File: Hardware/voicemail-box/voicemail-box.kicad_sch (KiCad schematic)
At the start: 13 parts, among them J1 Power, J2 Digital/PWM, J3 Analog, J4 Digital/PWM, J5 Conn_02x06_Top_Bottom, U1 ESP32-WROOM-32

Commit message: + gitignore ~ added existing pinout of sandbox tests
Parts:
- removed J1: Power, Connector_PinSocket_2.54mm:PinSocket_1x08_P2.54mm_Vertical, symbol Connector_Generic:Conn_01x08
- removed J2: Digital/PWM, Connector_PinSocket_2.54mm:PinSocket_1x10_P2.54mm_Vertical, symbol Connector_Generic:Conn_01x10
- removed J3: Analog, Connector_PinSocket_2.54mm:PinSocket_1x06_P2.54mm_Vertical, symbol Connector_Generic:Conn_01x06
- removed J4: Digital/PWM, Connector_PinSocket_2.54mm:PinSocket_1x08_P2.54mm_Vertical, symbol Connector_Generic:Conn_01x08
- added C3: 100n, Capacitor_SMD:C_0805_2012Metric_Pad1.18x1.45mm_HandSolder, symbol Device:C
- added CN1: ~, Connector_PinSocket_2.54mm:PinSocket_2x15_P2.54mm_Vertical, symbol myParts:NUCLEO_144_Analog+
- added CN2: ~, Connector_PinSocket_2.54mm:PinSocket_2x17_P2.54mm_Vertical, symbol myParts:NUCLEO_144_GPIO+
- added CN3: ~, Connector_PinSocket_2.54mm:PinSocket_2x10_P2.54mm_Vertical, symbol myParts:NUCLEO_144_Periphery+
- added CN4: ~, Connector_PinSocket_2.54mm:PinSocket_2x08_P2.54mm_Vertical, symbol myParts:NUCLEO_144_Power
- added J6: Micro_SD_Card_Det1, symbol Connector:Micro_SD_Card_Det1
- added RN3: 10k, Resistor_SMD:R_Array_Convex_4x0603, symbol Device:R_Pack04
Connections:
- net +3V3: now also C3.1, CN4.1 (NC), CN4.5 (NRST), J6.4 (VDD), RN3.1 (R1.1), RN3.2 (R2.1), RN3.3 (R3.1), RN3.4 (R4.1)
- net +5V: now also CN4.7 (+3V3)
- net AREF: now also CN3.6 (VREFP)
- net D2: now also CN2.12 (D2)
- net D3: now also CN2.10 (D3)
- net D4: now also CN2.8 (D4)
- net D5: now also CN2.6 (D5)
- net D6: now also CN2.4 (D6)
- net D8: now also CN3.20 (D8)
- net D9: now also CN3.18 (D9)
- net GND: now also C3.2, CN1.12 (GND), CN1.23 (GND), CN2.17 (GND), CN2.22 (GND), CN2.27 (GND), CN2.3 (AGND), CN2.5 (GND), CN3.8 (GND), CN4.11 (GND), CN4.9 (+5V), J6.10 (SHIELD), J6.6 (VSS)
- net RX/D0: now also CN2.16 (D0)
- net TX/D1: now also CN2.14 (D1)
- net VCC: now also CN4.13 (GND)
- net ~{RESET}: now also CN4.3 (IOREF)
- new net NFC_LED1: CN1.3 (A1)
- new net NFC_LED2: CN1.5 (A2)
- new net NFC_LED3: CN1.7 (A3)
- new net NFC_LED4: CN1.9 (A4)
- new net NFC_LED5: CN1.11 (A5)
- new net NFC_LED6: CN2.2 (D7)
- new net NFC_MISO: CN3.12 (D12)
- new net NFC_MOSI: CN3.14 (D11)
- new net NFC_NSS: CN3.16 (D10)
- new net NFC_SCK: CN3.10 (D13)
- new net NFT_INT: CN1.1 (A0)
- new net SCL: CN3.2 (D15)
- new net SDA: CN3.4 (D14)
- new net SD_CLK: CN4.10 (D47), J6.5 (CLK)
- new net SD_CMD: CN4.12 (D48), J6.3 (CMD)
- new net SD_DAT0: CN4.2 (D43), J6.7 (DAT0), RN3.5 (R4.2)
- new net SD_DAT1: CN4.4 (D44), J6.8 (DAT1), RN3.6 (R3.2)
- new net SD_DAT2: CN4.6 (D45), J6.1 (DAT2), RN3.7 (R2.2)
- new net SD_DAT3: CN4.8 (D46), J6.2 (DAT3/CD), RN3.8 (R1.2)
- new net SD_DET: CN4.14 (D49), J6.9 (DET)
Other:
- note added: "ESD-Protection for production Version required"
- note added: "F469 | H755"
- note added: "H755"
- note added: "Left out for ease of soldering for inexperienced users"
- note added: "Micro SD-Card"
- note added: "PA3 | PB1"
- note added: "PA5 | PD3"
- note added: "PA6 | PB14"
- note added: "PB1 | PC4"
- note added: "PB5 | PB15"
- note added: "PB8 | PB8"
- note added: "PB9 | PB9"
- note added: "PC0 | PC2"
- note added: "PC10"
- note added: "PC11"
- note added: "PC12"
- note added: "PC2 | PC5"
- note added: "PC3 | PC3"
- note added: "PC8"
- note added: "PC9"
- note added: "PD14 | PH6"
- note added: "PD2"
- note added: "PF11 | PA4"
- note added: "PG10"
- note added: "PG12 | PG11"
- note removed: "* Indicates a PWM-capable pin"
- note removed: "A0 | PA3 | PB1"
- note removed: "A1 | PC0 | PC2"
- note removed: "A2 | PC3 | PC3"
- note removed: "A3 | PB1 | PC4"
- note removed: "A4 | PC2 | PC5"
- note removed: "A5 | PF11 | PA4"
- note removed: "D14 | PB9 | PB9"
- note removed: "D15 | PB8 | PB8"

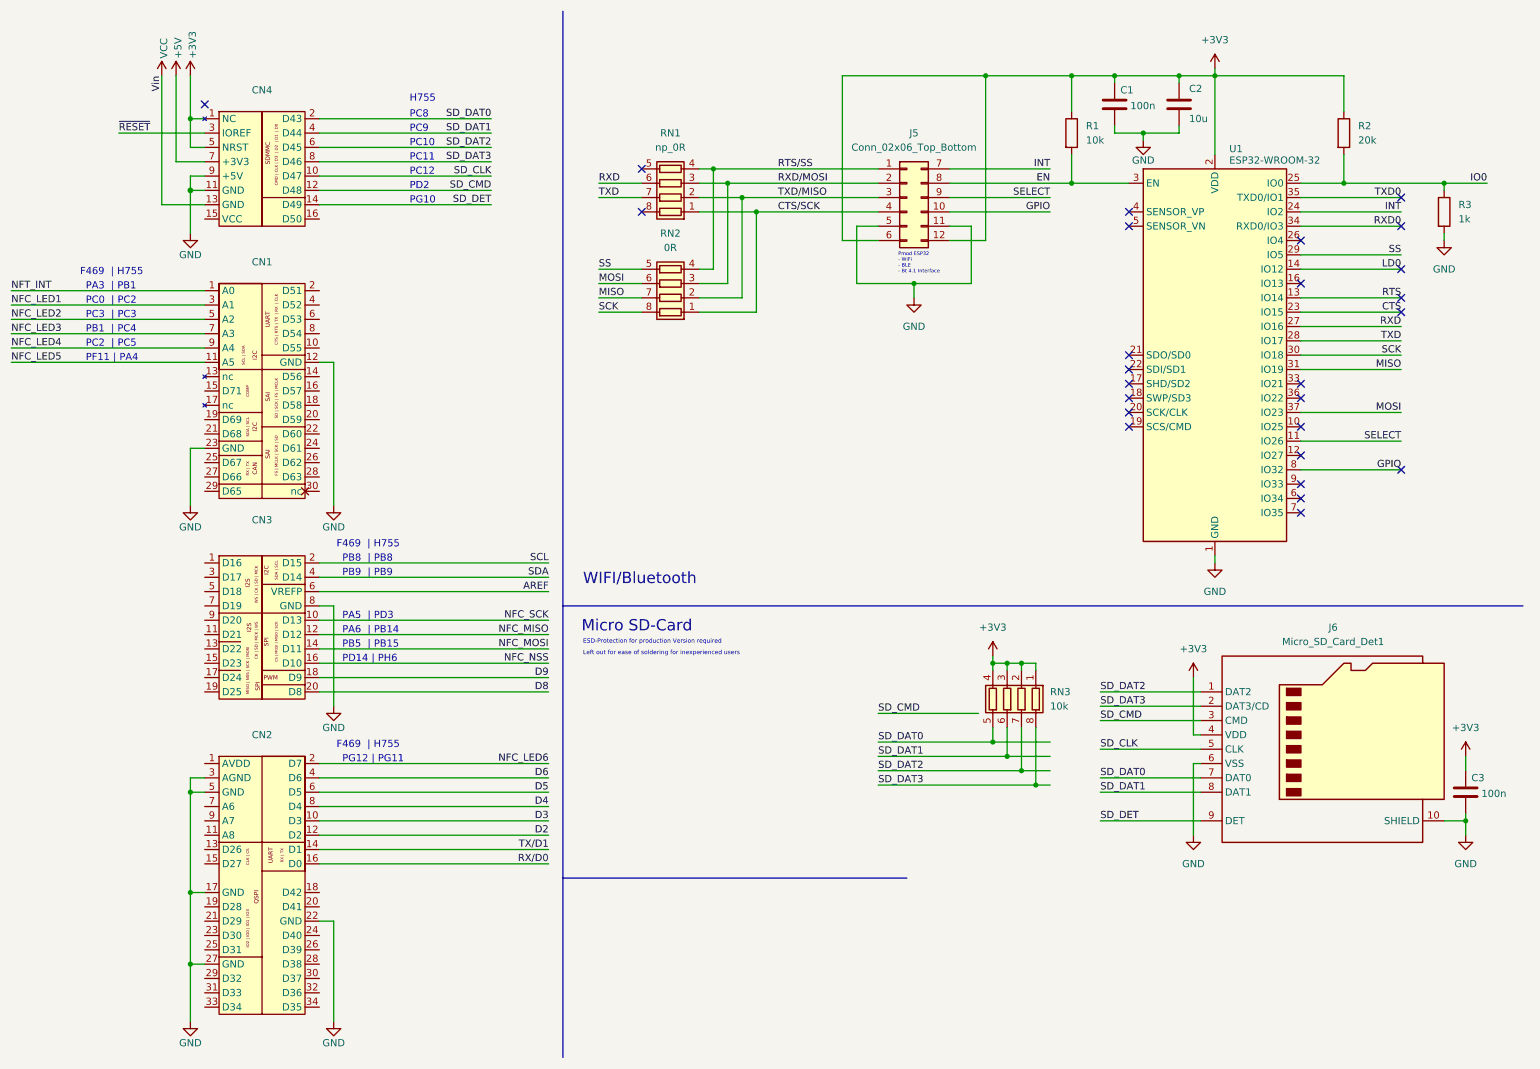
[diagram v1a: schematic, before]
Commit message: ~changed to hierarchical schematic
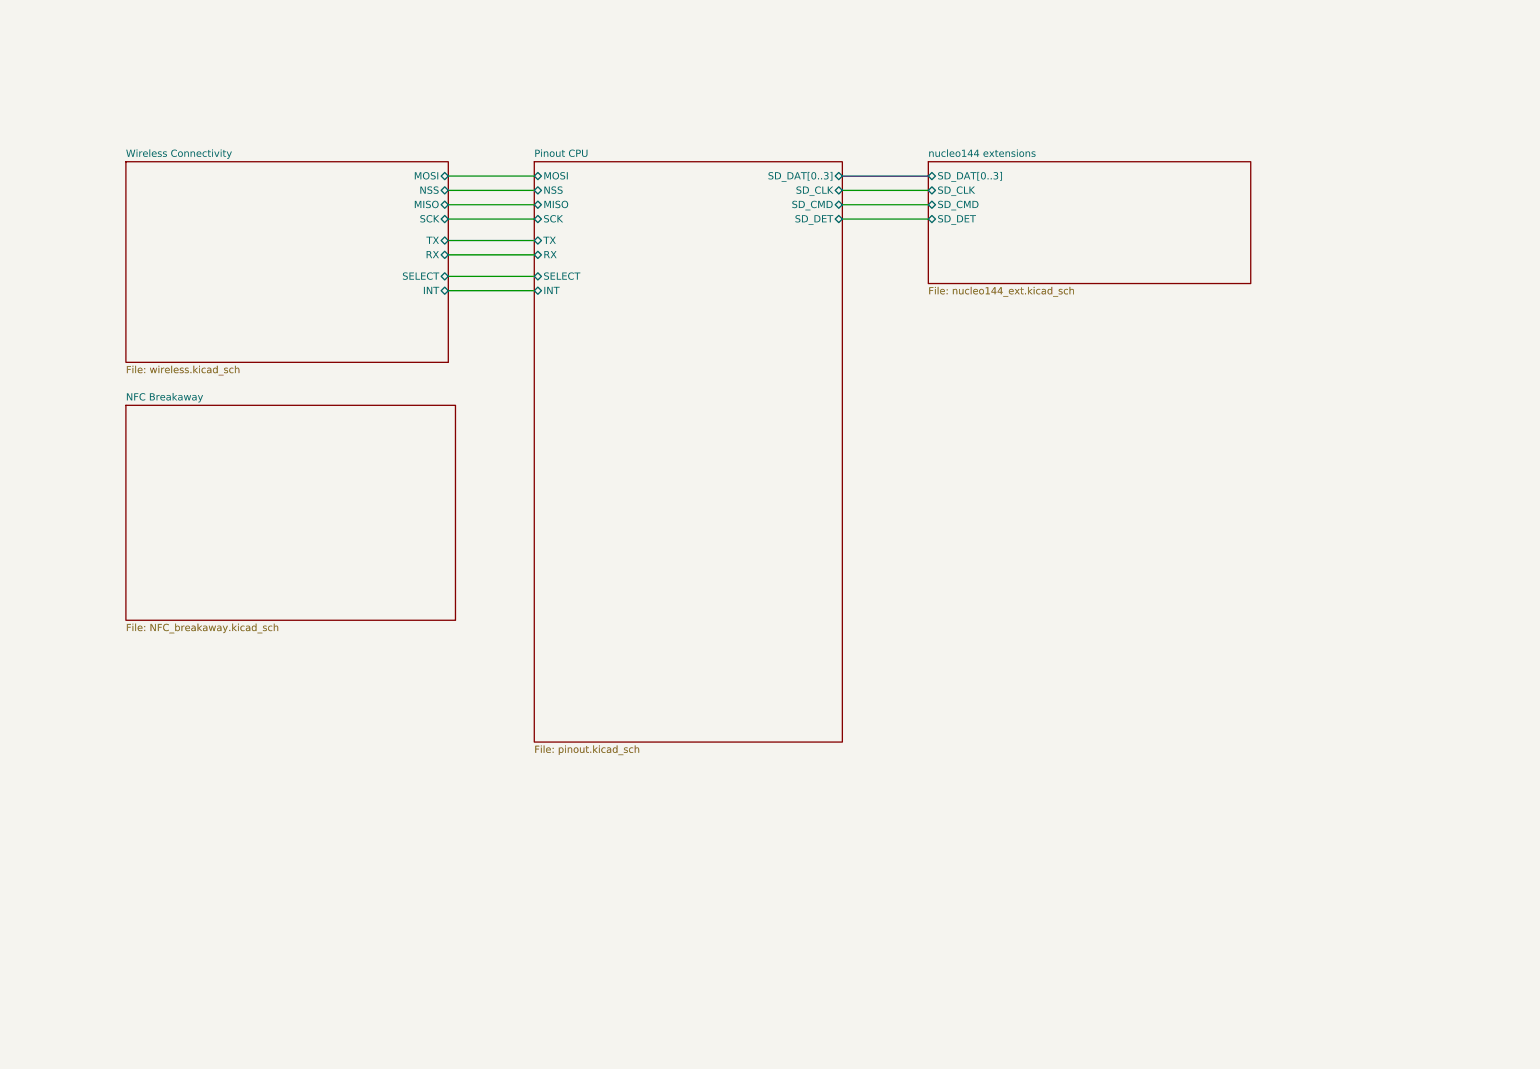
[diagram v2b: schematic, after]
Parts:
- removed C1, C3: 100n, Capacitor_SMD:C_0805_2012Metric_Pad1.18x1.45mm_HandSolder, symbol Device:C
- removed C2: 10u, Capacitor_SMD:C_0805_2012Metric_Pad1.18x1.45mm_HandSolder, symbol Device:C
- removed CN1: ~, Connector_PinSocket_2.54mm:PinSocket_2x15_P2.54mm_Vertical, symbol myParts:NUCLEO_144_Analog+
- removed CN2: ~, Connector_PinSocket_2.54mm:PinSocket_2x17_P2.54mm_Vertical, symbol myParts:NUCLEO_144_GPIO+
- removed CN3: ~, Connector_PinSocket_2.54mm:PinSocket_2x10_P2.54mm_Vertical, symbol myParts:NUCLEO_144_Periphery+
- removed CN4: ~, Connector_PinSocket_2.54mm:PinSocket_2x08_P2.54mm_Vertical, symbol myParts:NUCLEO_144_Power
- removed J5: Conn_02x06_Top_Bottom, Connector_PinHeader_2.54mm:PinHeader_2x06_P2.54mm_Horizontal, symbol Connector_Generic:Conn_02x06_Top_Bottom
- removed J6: Micro_SD_Card_Det1, symbol Connector:Micro_SD_Card_Det1
- removed R1: 10k, Resistor_SMD:R_0805_2012Metric_Pad1.20x1.40mm_HandSolder, symbol Device:R
- removed R2: 20k, Resistor_SMD:R_0805_2012Metric_Pad1.20x1.40mm_HandSolder, symbol Device:R
- removed R3: 1k, Resistor_SMD:R_0805_2012Metric_Pad1.20x1.40mm_HandSolder, symbol Device:R
- removed RN1: np_0R, Resistor_SMD:R_Array_Convex_4x0603, symbol Device:R_Pack04
- removed RN2: 0R, Resistor_SMD:R_Array_Convex_4x0603, symbol Device:R_Pack04
- removed RN3: 10k, Resistor_SMD:R_Array_Convex_4x0603, symbol Device:R_Pack04
- removed U1: ESP32-WROOM-32, RF_Module:ESP32-WROOM-32, symbol RF_Module:ESP32-WROOM-32
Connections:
- no-connect marks 26 -> 0
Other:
- added sheet NFC Breakaway (NFC_breakaway.kicad_sch)
- added sheet Pinout CPU (pinout.kicad_sch)
- added sheet Wireless Connectivity (wireless.kicad_sch)
- added sheet nucleo144 extensions (nucleo144_ext.kicad_sch)
- note removed: "ESD-Protection for production Version required"
- note removed: "F469 | H755"
- note removed: "H755"
- note removed: "Left out for ease of soldering for inexperienced users"
- note removed: "Micro SD-Card"
- note removed: "PA3 | PB1"
- note removed: "PA5 | PD3"
- note removed: "PA6 | PB14"
- note removed: "PB1 | PC4"
- note removed: "PB5 | PB15"
- note removed: "PB8 | PB8"
- note removed: "PB9 | PB9"
- note removed: "PC0 | PC2"
- note removed: "PC10"
- note removed: "PC11"
- note removed: "PC12"
- note removed: "PC2 | PC5"
- note removed: "PC3 | PC3"
- note removed: "PC8"
- note removed: "PC9"
- note removed: "PD14 | PH6"
- note removed: "PD2"
- note removed: "PF11 | PA4"
- note removed: "PG10"
- note removed: "PG12 | PG11"
- note removed: "Pmod ESP32 - WiFi - BLE - Bt 4.1 Interface"
- note removed: "WIFI/Bluetooth"

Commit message: ~ HW Configuration
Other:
- added sheet Analog (analog.kicad_sch)
- sheet NFC Breakaway ports: added NFC_INT, NFC_MISO, NFC_MOSI, NFC_NSS, NFC_SCK; removed none
- sheet Pinout CPU ports: added NFC_INT, NFC_MISO, NFC_MOSI, NFC_NSS, NFC_SCK; removed none
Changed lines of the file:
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@@
+	(wire
+		(pts
+			(xy 95.25 85.09) (xy 109.22 85.09)
+		)
+		(stroke
+			(width 0)
+			(type default)
+		)
+	)
+	(wire
+		(pts
+			(xy 95.25 90.17) (xy 109.22 90.17)
+		)
+		(stroke
+			(width 0)
+			(type default)
+		)
+	)
 	(wire
 		(pts
@@
 	(wire
 		(pts
+			(xy 95.25 95.25) (xy 109.22 95.25)
+		)
+		(stroke
+			(width 0)
+			(type default)
+		)
+	)
+	(wire
+		(pts
 			(xy 93.98 62.23) (xy 109.22 62.23)
 		)
@@
 	(wire
 		(pts
+			(xy 95.25 87.63) (xy 109.22 87.63)
+		)
+		(stroke
+			(width 0)
+			(type default)
+		)
+	)
+	(wire
+		(pts
 			(xy 163.83 46.99) (xy 179.07 46.99)
 		)
@@
 	(wire
 		(pts
+			(xy 95.25 92.71) (xy 109.22 92.71)
+		)
+		(stroke
+			(width 0)
+			(type default)
+		)
+	)
+	(wire
+		(pts
 			(xy 93.98 44.45) (xy 109.22 44.45)
 		)
@@
 			(width 0)
 			(type default)
+		)
+	)
+	(sheet
+		(at 179.07 74.93)
+		(size 57.15 21.59)
+		(exclude_from_sim no)
+		(in_bom yes)
+		(on_board yes)
+		(dnp no)
+		(fields_autoplaced yes)
+		(stroke
+			(width 0.1524)
+			(type solid)
+		)
+		(fill
+			(color 0 0 0 0.0000)
+		)
+		(property "Sheetname" "Analog"
+			(at 179.07 74.2184 0)
+			(effects
+				(font
+					(size 1.27 1.27)
+				)
+				(justify left bottom)
+			)
+		)
+		(property "Sheetfile" "analog.kicad_sch"
+			(at 179.07 97.1046 0)
+			(effects
+				(font
+					(size 1.27 1.27)
+				)
+				(justify left top)
+			)
+		)
+		(instances
+			(project "voicemail-box"
+				(path "/e63e39d7-6ac0-4ffd-8aa3-1841a4541b55"
+					(page "6")
+				)
+			)
 		)
 	)
@@
 			)
 		)
+		(pin "NFC_MISO" bidirectional
+			(at 109.22 95.25 180)
+			(effects
+				(font
+					(size 1.27 1.27)
+				)
+				(justify left)
+			)
+		)
+		(pin "NFC_MOSI" bidirectional
+			(at 109.22 85.09 180)
+			(effects
+				(font
+					(size 1.27 1.27)
+				)
+				(justify left)
+			)
+		)
+		(pin "NFC_SCK" bidirectional
+			(at 109.22 87.63 180)
+			(effects
+				(font
+					(size 1.27 1.27)
+				)
+				(justify left)
+			)
+		)
+		(pin "NFC_INT" bidirectional
+			(at 109.22 92.71 180)
+			(effects
+				(font
+					(size 1.27 1.27)
+				)
+				(justify left)
+			)
+		)
+		(pin "NFC_NSS" bidirectional
+			(at 109.22 90.17 180)
+			(effects
+				(font
+					(size 1.27 1.27)
+				)
+				(justify left)
+			)
+		)
 		(instances
 			(project "voicemail-box"
@@
 			)
 		)
+		(pin "NFC_MOSI" bidirectional
+			(at 95.25 85.09 0)
+			(effects
+				(font
+					(size 1.27 1.27)
+				)
+				(justify right)
+			)
+		)
+		(pin "NFC_SCK" bidirectional
+			(at 95.25 87.63 0)
+			(effects
+				(font
+					(size 1.27 1.27)
+				)
+				(justify right)
+			)
+		)
+		(pin "NFC_NSS" bidirectional
+			(at 95.25 90.17 0)
+			(effects
+				(font
+					(size 1.27 1.27)
+				)
+				(justify right)
+			)
+		)
+		(pin "NFC_INT" bidirectional
+			(at 95.25 92.71 0)
+			(effects
+				(font
+					(size 1.27 1.27)
+				)
+				(justify right)
+			)
+		)
+		(pin "NFC_MISO" bidirectional
+			(at 95.25 95.25 0)
+			(effects
+				(font
+					(size 1.27 1.27)
+				)
+				(justify right)
+			)
+		)

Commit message: -
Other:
- added sheet Powersupply (powersupply.kicad_sch)
- sheet Analog ports: added CODEC_I2C_SCL, CODEC_I2C_SDA, CODEC_I2S_BCLK, CODEC_I2S_DIN, CODEC_I2S_DOUT, CODEC_I2S_MCLK, CODEC_I2S_WCLK, CODEC_nRESET; removed none
- sheet Pinout CPU ports: added CODEC_nRESET, I2C_SCL, I2C_SDA, I2S2_BCLK, I2S2_MCLK, I2S2_SDA, I2S2_SDA_ext, I2S2_WCLK, SPI1_MISO, SPI1_MOSI, SPI1_NSS, SPI1_SCK; removed NFC_MISO, NFC_MOSI, NFC_NSS, NFC_SCK
- note added: "Data Dir?"
- note added: "Jumper for 144"
- note added: "Jumper for SPI/USRT"

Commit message: schematic draft
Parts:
- added J101, J103: Conn_02x08_Odd_Even, Connector_PinHeader_2.54mm:PinHeader_2x08_P2.54mm_Vertical, symbol Connector_Generic:Conn_02x08_Odd_Even
- added J102: Conn_02x03_Odd_Even, Connector_PinSocket_2.54mm:PinSocket_2x03_P2.54mm_Vertical, symbol Connector_Generic:Conn_02x03_Odd_Even
- added R101, R102, R103: 4k7, PCM_4ms_Resistor:R_0603, symbol Device:R
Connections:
- net Audio/CODEC_I2C_SCL: now also J102.6 (Pin_6), R102.2
- net Audio/CODEC_I2C_SDA: now also J102.4 (Pin_4), R101.2
- net NFC Breakaway/NFC_MISO: now also J101.16 (Pin_16), J101.8 (Pin_8), J102.3 (Pin_3)
- net NFC Breakaway/NFC_MOSI: now also J101.10 (Pin_10), J101.2 (Pin_2)
- net NFC Breakaway/NFC_NSS: now also J101.14 (Pin_14), J101.6 (Pin_6)
- net NFC Breakaway/NFC_SCK: now also J101.12 (Pin_12), J101.4 (Pin_4), J102.5 (Pin_5)
- net Pinout CPU/MISO: now also J103.6 (Pin_6)
- net Pinout CPU/MOSI: now also J103.2 (Pin_2)
- net Pinout CPU/NSS: now also J103.4 (Pin_4)
- net Pinout CPU/RX: now also J103.14 (Pin_14)
- net Pinout CPU/SCK: now also J103.8 (Pin_8)
- net Pinout CPU/SPI1_MISO: now also J101.7 (Pin_7)
- net Pinout CPU/SPI1_MOSI: now also J101.1 (Pin_1)
- net Pinout CPU/SPI1_NSS: now also J101.5 (Pin_5)
- net Pinout CPU/SPI1_SCK: now also J101.3 (Pin_3)
- net Pinout CPU/TX: now also J103.12 (Pin_12)
- net Wireless Connectivity/MISO: now also J103.5 (Pin_5)
- net Wireless Connectivity/MOSI: now also J103.1 (Pin_1)
- net Wireless Connectivity/NSS: now also J103.3 (Pin_3)
- net Wireless Connectivity/RX: now also J103.13 (Pin_13)
- net Wireless Connectivity/SCK: now also J103.7 (Pin_7)
- net Wireless Connectivity/TX: now also J103.11 (Pin_11)
- new net +3.3V: J103.16 (Pin_16), R101.1, R102.1
- new net GND: J102.1 (Pin_1), R103.2
- new net NFC Breakaway/I2C_Disable: J102.2 (Pin_2)
- new net Pinout CPU/SPI2_MISO: J101.15 (Pin_15)
- new net Pinout CPU/SPI2_MOSI: J101.9 (Pin_9)
- new net Pinout CPU/SPI2_NSS: J101.13 (Pin_13)
- new net Pinout CPU/SPI2_SCK: J101.11 (Pin_11)
- new net Wireless Connectivity/SELECT: J103.15 (Pin_15), R103.1
- no-connect marks 0 -> 2
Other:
- sheet Analog renamed Audio
- added sheet User Interface (userinterface.kicad_sch)
- sheet NFC Breakaway ports: added I2C_Disable; removed none
- sheet Pinout CPU ports: added SPI2_MISO, SPI2_MOSI, SPI2_NSS, SPI2_SCK; removed SELECT
- note added: "J101: -------------------------------- SPI_F469 |SPI_H755 |no SPI con | - set |- open |- open | - set |- open |- open | - set |- open |- open | - set |- open |- open | - open |- set |- open | - open |- set |- open | - open |- set |- open | - open |- set |- open |"
- note added: "J102: ------------------ SPI |I2C | - open |- set | - open |- set | - set |- open |"
- note added: "J103: ------------------ SPI |I2C | - set |- open | - set |- open | - set |- open | - set |- open | | | - open |- set | - open |- set | - open |- set |"
- note removed: "Jumper for 144"
- note removed: "Jumper for SPI/USRT"

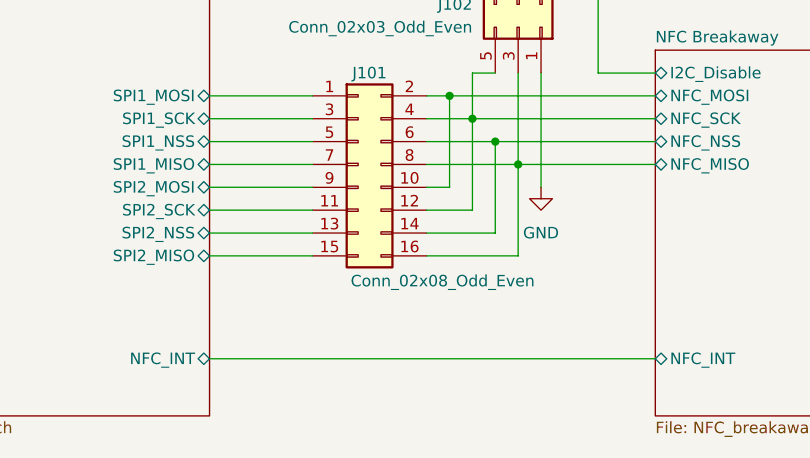
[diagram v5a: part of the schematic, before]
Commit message: corrected pinout to nucleo description
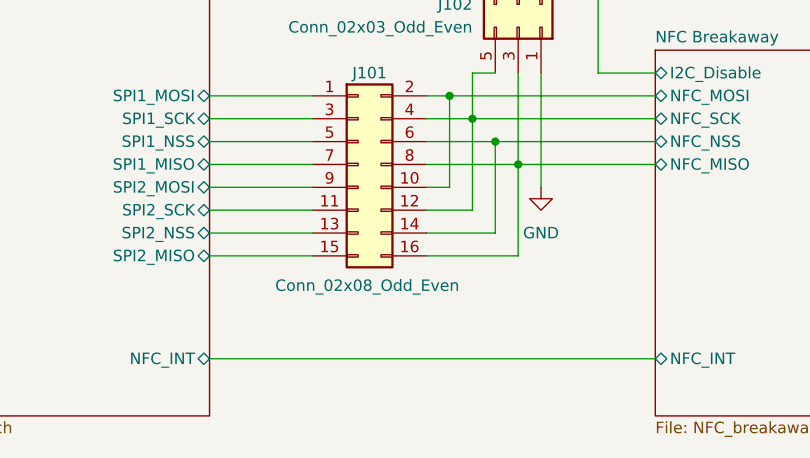
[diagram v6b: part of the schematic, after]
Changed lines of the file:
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@@
 		)
 		(property "Value" "Conn_02x08_Odd_Even"
-			(at 175.768 137.414 0)
+			(at 167.386 137.922 0)
 			(effects
 				(font
